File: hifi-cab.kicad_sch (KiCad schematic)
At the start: 33 parts, among them J1 FAN 1, J10 BUTTON, J11 RS-232, J12 VOLTAGE_SEL, J13 PWR IN, J2 FAN VOLTAGE, J3 FAN 1, J4 FAN 2, J5 FAN VOLTAGE, J6 FAN 2, J7 IR REMOTE, J8 DS18B20, J9 DS18B20, Q1 AO3400A, Q2 AO3400A, Q3 AO3400A, U1 esp32-wemos-d1-mini, U2 TSR1-2433E

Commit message: Start layout
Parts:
- R9: footprint Resistor_SMD:R_0805_2012Metric_Pad1.20x1.40mm_HandSolder -> Resistor_THT:R_Axial_DIN0204_L3.6mm_D1.6mm_P5.08mm_Horizontal
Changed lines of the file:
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@@
 			)
 		)
-		(property "Footprint" "Resistor_SMD:R_0805_2012Metric_Pad1.20x1.40mm_HandSolder"
+		(property "Footprint" "Resistor_THT:R_Axial_DIN0204_L3.6mm_D1.6mm_P5.08mm_Horizontal"
 			(at 86.36 169.418 90)
 			(effects

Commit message: Moar layout
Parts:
- added C1: 400uF, symbol Device:C_Polarized
- J12: value VOLTAGE_SEL -> 5V ENABLE; symbol Connector:Conn_01x03_Pin -> Connector:Conn_01x02_Pin
- J2, J5: footprint Connector_PinHeader_2.54mm:PinHeader_1x02_P2.54mm_Vertical -> Connector_PinHeader_2.54mm:PinHeader_1x03_P2.54mm_Vertical
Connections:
- net +5V: no longer U1.35 (VCC_(USB))
- net GND: now also C1.2
- net VCC: now also J12.2 (Pin_2), J13.1 (Pin_1), C1.1; no longer J12.3 (Pin_3)
- no-connect marks 25 -> 26

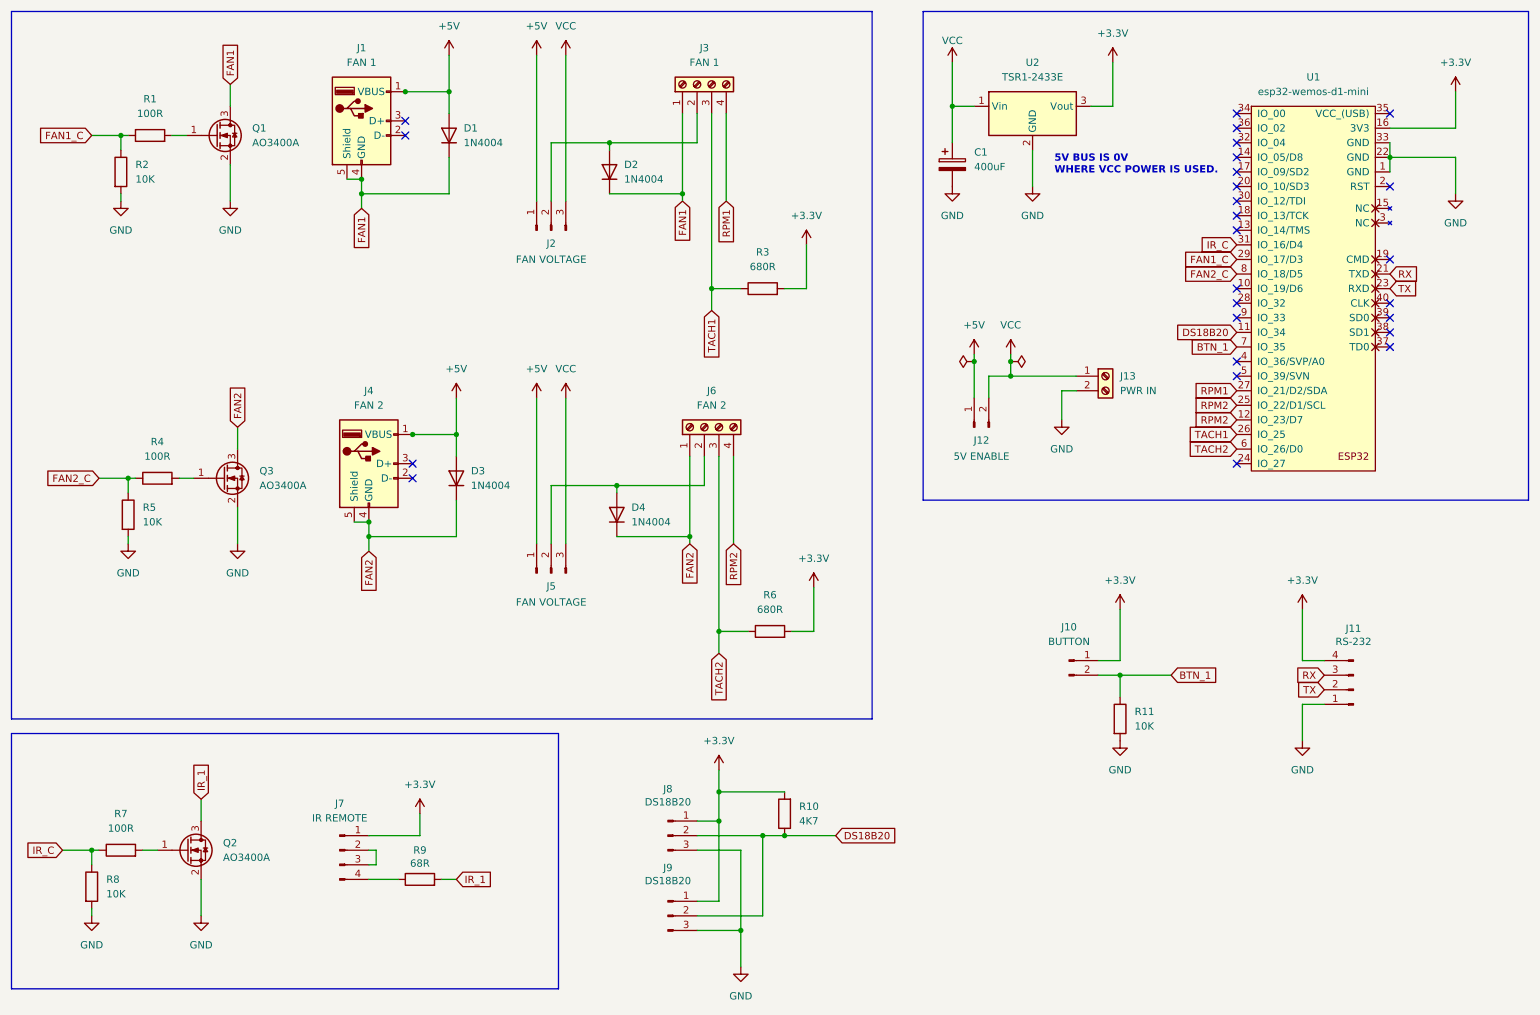
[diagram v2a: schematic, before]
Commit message: Simplify, return to 5V only.
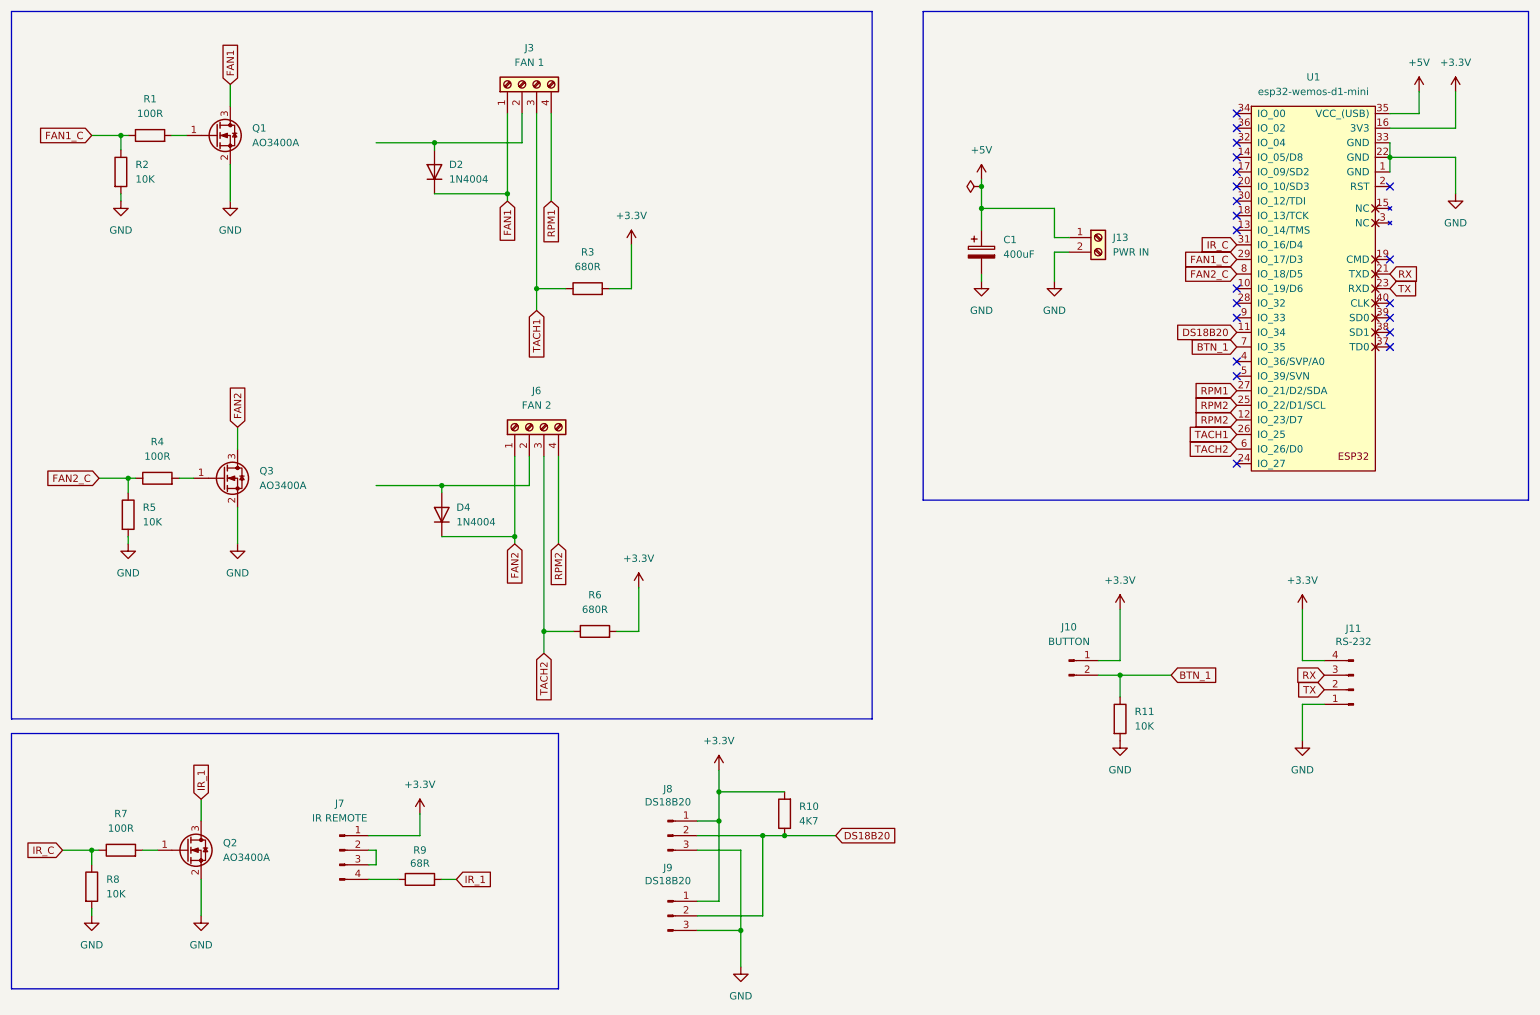
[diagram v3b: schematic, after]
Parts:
- removed D1, D3: 1N4004, Diode_THT:D_DO-41_SOD81_P10.16mm_Horizontal, symbol Diode:1N4004
- removed J1: FAN 1, USB_A1VSB6:ONSHORE_USB-A1VSB6, symbol Connector:USB_A
- removed J12: 5V ENABLE, Connector_PinHeader_2.54mm:PinHeader_1x02_P2.54mm_Vertical, symbol Connector:Conn_01x02_Pin
- removed J2, J5: FAN VOLTAGE, Connector_PinHeader_2.54mm:PinHeader_1x03_P2.54mm_Vertical, symbol Connector:Conn_01x03_Pin
- removed J4: FAN 2, USB_A1VSB6:ONSHORE_USB-A1VSB6, symbol Connector:USB_A
- removed U2: TSR1-2433E, Converter_DCDC:Converter_DCDC_TRACO_TSR1-xxxxE_THT, symbol Converter_DCDC:TSR1-2433E
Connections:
- net VCC is gone; now on net +5V: C1.1, J13.1 (Pin_1)
- net +5V: now also U1.35 (VCC_(USB))
- no-connect marks 26 -> 21
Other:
- note removed: "5V BUS IS 0V WHERE VCC POWER IS USED."
- moved on the sheet: C1, D2, D4, J13, J3, J6, R3, R6

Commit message: Add cap
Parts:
- C1: footprint (none) -> Capacitor_THT:CP_Radial_D5.0mm_P2.50mm
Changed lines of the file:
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@@
 			)
 		)
-		(property "Footprint" ""
+		(property "Footprint" "Capacitor_THT:CP_Radial_D5.0mm_P2.50mm"
 			(at 185.1152 62.23 0)
 			(effects

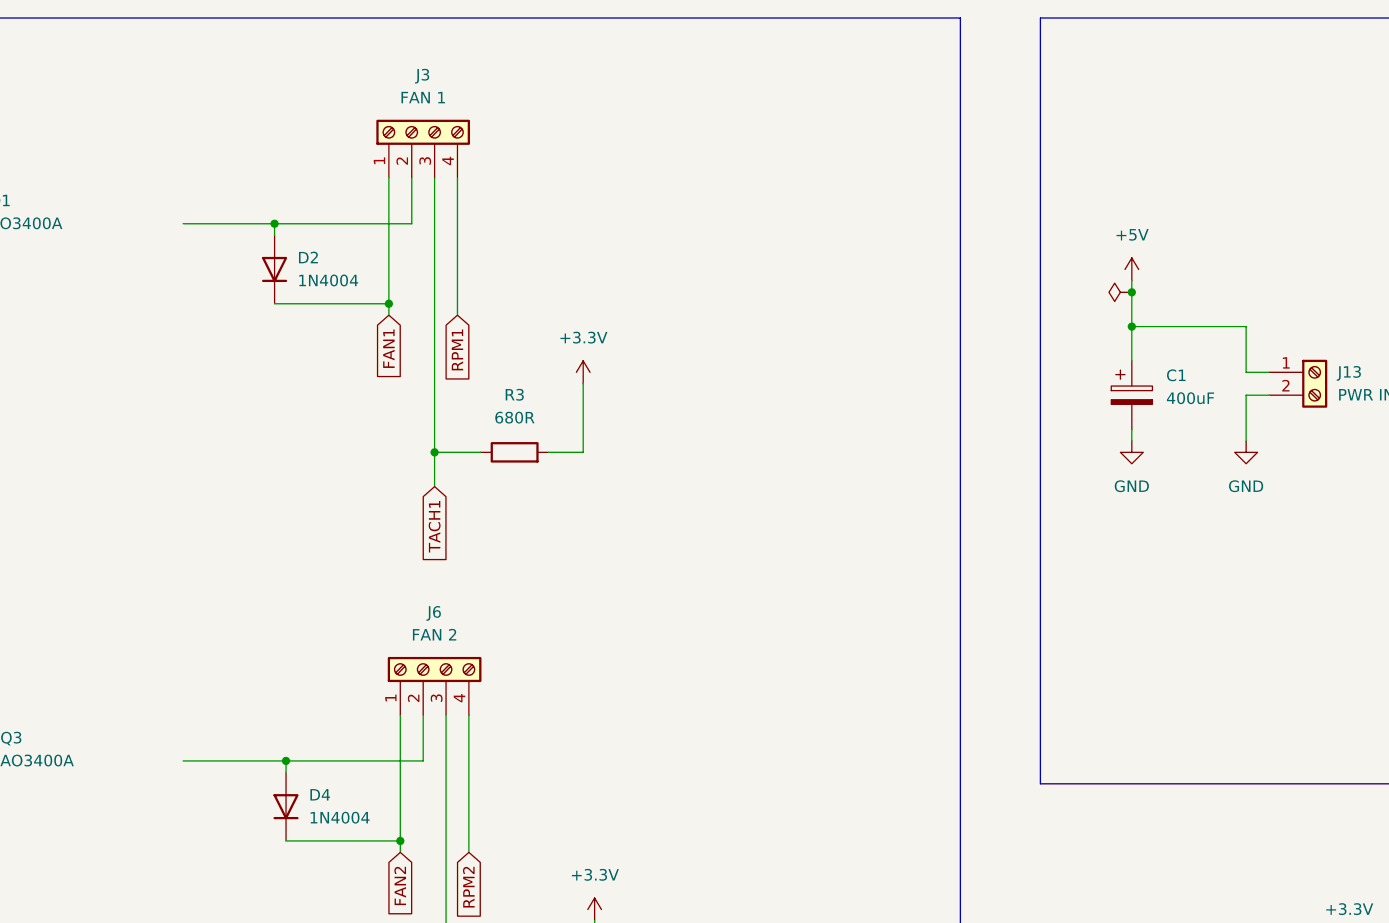
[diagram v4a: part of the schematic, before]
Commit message: Fix power on schematic
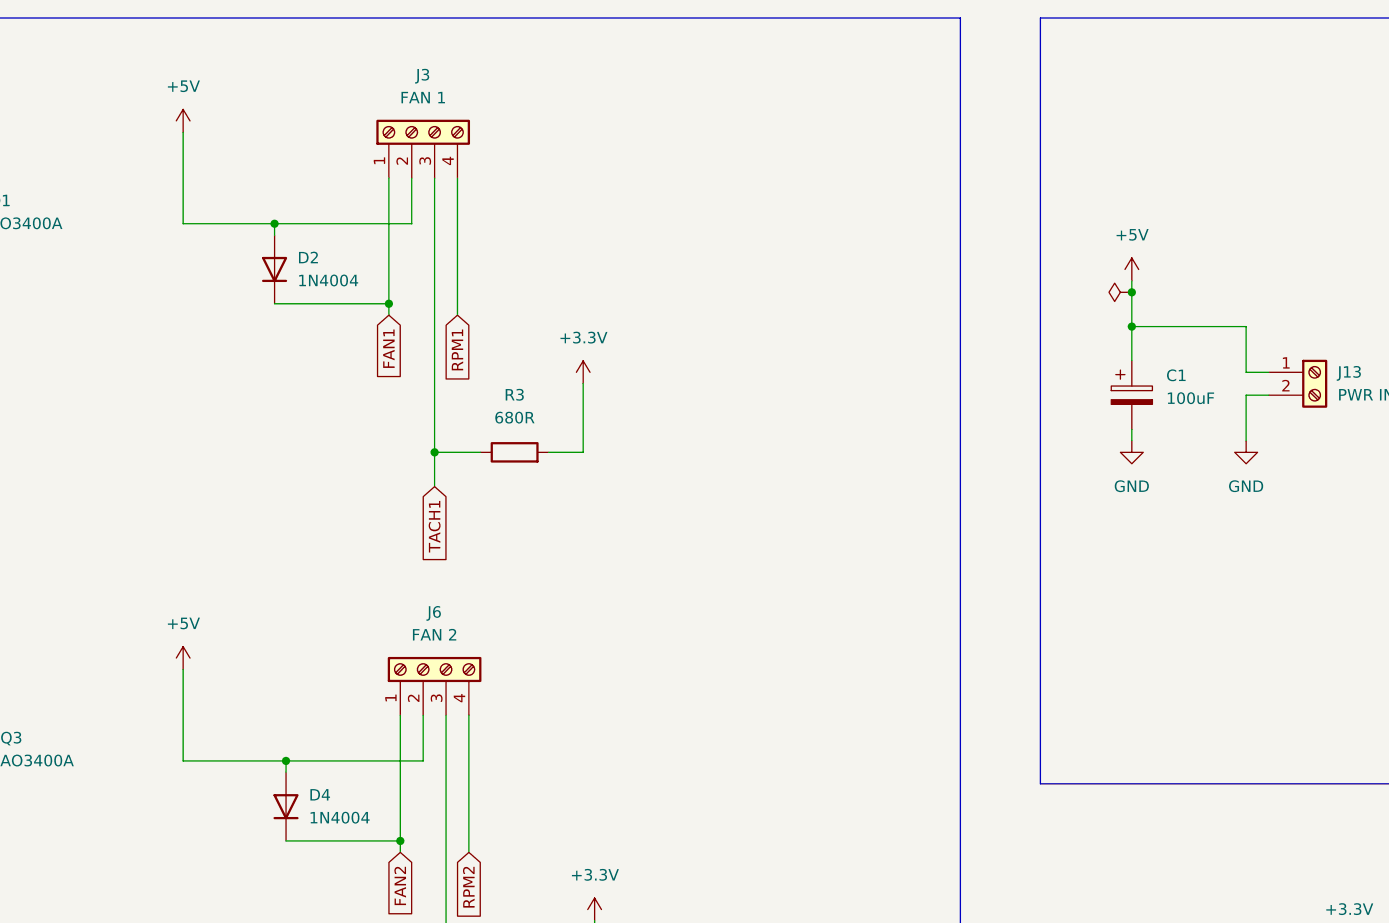
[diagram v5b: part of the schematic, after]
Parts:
- C1: value 400uF -> 100uF
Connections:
- net +5V: now also D2.2 (A), D4.2 (A), J3.2 (Pin_2), J6.2 (Pin_2)
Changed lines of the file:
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@@
 	(wire
 		(pts
+			(xy 78.74 29.21) (xy 78.74 39.37)
+		)
+		(stroke
+			(width 0)
+			(type default)
+		)
+	)
+	(wire
+		(pts
 			(xy 35.56 107.95) (xy 35.56 109.22)
 		)
@@
 	(wire
 		(pts
+			(xy 78.74 88.9) (xy 78.74 99.06)
+		)
+		(stroke
+			(width 0)
+			(type default)
+		)
+	)
+	(wire
+		(pts
 			(xy 43.18 38.1) (xy 45.72 38.1)
 		)
@@
 	)
 	(symbol
+		(lib_id "power:+5V")
+		(at 78.74 88.9 0)
+		(unit 1)
+		(exclude_from_sim no)
+		(in_bom yes)
+		(on_board yes)
+		(dnp no)
+		(fields_autoplaced yes)
+		(property "Reference" "#PWR05"
+			(at 78.74 92.71 0)
+			(effects
+				(font
+					(size 1.27 1.27)
+				)
+				(hide yes)
+			)
+		)
+		(property "Value" "+5V"
+			(at 78.74 83.82 0)
+			(effects
+				(font
+					(size 1.27 1.27)
+				)
+			)
+		)
+		(property "Footprint" ""
+			(at 78.74 88.9 0)
+			(effects
+				(font
+					(size 1.27 1.27)
+				)
+				(hide yes)
+			)
+		)
+		(property "Datasheet" ""
+			(at 78.74 88.9 0)
+			(effects
+				(font
+					(size 1.27 1.27)
+				)
+				(hide yes)
+			)
+		)
+		(property "Description" "Power symbol creates a global label with name \"+5V\""
+			(at 78.74 88.9 0)
+			(effects
+				(font
+					(size 1.27 1.27)
+				)
+				(hide yes)
+			)
+		)
+		(pin "1"
+		)
+		(instances
+			(project "hifi-cab"
+				(path "/464ef4ad-8e38-4b55-beb7-b05b4d6675da"
+					(reference "#PWR05")
+					(unit 1)
+				)
+			)
+		)
+	)
+	(symbol
 		(lib_id "Device:C_Polarized")
 		(at 184.15 58.42 0)
@@
 			)
 		)
-		(property "Value" "400uF"
+		(property "Value" "100uF"
 			(at 187.96 58.8009 0)
 			(effects
@@
 					(unit 1)
 				)
+			)
+		)
+	)
+	(symbol
+		(lib_id "power:+5V")
+		(at 78.74 29.21 0)
+		(unit 1)
+		(exclude_from_sim no)
+		(in_bom yes)
+		(on_board yes)
+		(dnp no)
+		(fields_autoplaced yes)
+		(property "Reference" "#PWR04"
+			(at 78.74 33.02 0)
+			(effects
+				(font
+					(size 1.27 1.27)
+				)
+				(hide yes)
+			)
+		)
+		(property "Value" "+5V"
+			(at 78.74 24.13 0)
+			(effects
+				(font
+					(size 1.27 1.27)
+				)
+			)
+		)
+		(property "Footprint" ""
+			(at 78.74 29.21 0)
+			(effects
+				(font
+					(size 1.27 1.27)
+				)
+				(hide yes)
+			)
+		)
+		(property "Datasheet" ""
+			(at 78.74 29.21 0)
+			(effects
+				(font
+					(size 1.27 1.27)
+				)
+				(hide yes)
+			)
+		)
+		(property "Description" "Power symbol creates a global label with name \"+5V\""
+			(at 78.74 29.21 0)
+			(effects
+				(font
+					(size 1.27 1.27)
+				)
+				(hide yes)
+			)
+		)
+		(pin "1"
+		)
+		(instances
+			(project ""
+				(path "/464ef4ad-8e38-4b55-beb7-b05b4d6675da"
+					(reference "#PWR04")
+					(unit 1)
+				)

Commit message: Explore layout.
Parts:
- added U2: TSR0.5-2433, Converter_DCDC:Converter_DCDC_TRACO_TSR0.5-24xx_TSR0.5-24xxx_THT, symbol Converter_DCDC:TSR0.5-2433
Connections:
- net +3.3V: now also U2.3 (Vout)
- net GND: now also J13.1 (Pin_1), U2.2 (GND); no longer J13.2 (Pin_2)
- net +5V renamed VCC
- net VCC: now also J13.2 (Pin_2), U2.1 (Vin); no longer J13.1 (Pin_1), U1.35 (VCC_(USB))
- no-connect marks 21 -> 22
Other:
- moved on the sheet: C1, J13, U1

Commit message: Tidy footprints
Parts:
- removed J9: DS18B20, Connector_JST:JST_XH_B3B-XH-A_1x03_P2.50mm_Vertical, symbol Connector:Conn_01x03_Pin
- added D1: 1N4004, Diode_THT:D_DO-41_SOD81_P10.16mm_Horizontal, symbol Diode:1N4004
- added J7: FAN 3, Connector:FanPinHeader_1x04_P2.54mm_Vertical, symbol Connector:Screw_Terminal_01x04
- added Q4: AO3400A, Package_TO_SOT_SMD:SOT-23, symbol Transistor_FET:AO3400A
- added R6: 680R, Resistor_SMD:R_0805_2012Metric_Pad1.20x1.40mm_HandSolder, symbol Device:R
- added R7: 100R, Resistor_SMD:R_0805_2012Metric_Pad1.20x1.40mm_HandSolder, symbol Device:R
- added R8: 10K, Resistor_SMD:R_0805_2012Metric_Pad1.20x1.40mm_HandSolder, symbol Device:R
- renumbered D4 to D3, J13 to J1, J10 to J2, J11 to J3, J8 to J4, J7 to J5, J3 to J6, J6 to J8, R7 to R10, R8 to R11, R9 to R12, R10 to R13, R11 to R14, R6 to R9
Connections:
- net +3.3V: now also R6.2
- net GND: now also Q4.2 (S), R8.2
- net VCC: now also D1.2 (A), J7.2 (Pin_2)
- new net: Q4.1 (G), R7.2
- new net FAN3: D1.1 (K), J7.1 (Pin_1), Q4.3 (D)
- new net FAN3_C: R7.1, R8.1
- new net RPM3: J7.4 (Pin_4)
- new net TACH3: J7.3 (Pin_3), R6.1
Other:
- moved on the sheet: D2, D3, J6, J8, Q3, R3, R4, R5, R9

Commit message: More layout
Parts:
- removed J2: BUTTON, Connector_JST:JST_XH_B2B-XH-A_1x02_P2.50mm_Vertical, symbol Connector:Conn_01x02_Pin
- removed J5: IR REMOTE, Connector_JST:JST_XH_B4B-XH-A_1x04_P2.50mm_Vertical, symbol Connector:Conn_01x04_Pin
- removed R12: 68R, Resistor_THT:R_Axial_DIN0204_L3.6mm_D1.6mm_P5.08mm_Horizontal, symbol Device:R
- removed R14: 10K, Resistor_SMD:R_0805_2012Metric_Pad1.20x1.40mm_HandSolder, symbol Device:R
- added J1: IR, Connector_JST:JST_XH_B2B-XH-A_1x02_P2.50mm_Vertical, symbol Connector:Conn_01x02_Pin
- added R9: 68R, Resistor_THT:R_Axial_DIN0204_L3.6mm_D1.6mm_P5.08mm_Horizontal, symbol Device:R
- renumbered D2 to D1, D3 to D2, D1 to D3, J6 to J2, J8 to J3, J7 to J4, J4 to J5, J1 to J6, J3 to J7, Q2 to Q1, Q1 to Q2, R11 to R1, R3 to R10, R9 to R11, R6 to R12, R5 to R3, R8 to R4, R10 to R5, R1 to R6, R4 to R7, R7 to R8, U2 to U1, U1 to U2
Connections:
- net BTN_1 is gone; now on net FAN3_C: U2.7 (IO_35)
- net +3.3V: now also J1.2 (Pin_2)
- net IR_1: now also R9.2
- net RPM2: no longer U2.12 (IO_23/D7)
- net RPM3: now also U2.12 (IO_23/D7)
- net TACH3: now also U2.24 (IO_27)
- new net: J1.1 (Pin_1), R9.1
- no-connect marks 22 -> 21
